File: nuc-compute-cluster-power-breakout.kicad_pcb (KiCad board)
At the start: 4 copper layers, 100 x 100 mm, 159 parts, among them J1 USB3106-30-0230-A, J10 10107844-002LF, J2 BM04B-SRSS-TB-LF-SN, J3 BM04B-SRSS-TB-LF-SN, J4 43045-1013, J5 430450812, J6 430450812, J7 430450812, J8 430450812, J9 430450812, Q1 SQS401EN-T1_BE3, Q10 SSM3K15ACT, Q11 BC856,215, Q15 DMN4010LFG-7, Q2 SQS401EN-T1_BE3, Q3 SSM3K15ACT, Q4 SSM3K15ACT, Q5 SQS401EN-T1_BE3, Q6 SSM3K15ACT, Q7 SQS401EN-T1_BE3, Q8 SQS401EN-T1_BE3, Q9 SSM3K15ACT, U1 FT2232HL-REEL, U10 TCA9534, U11 TMCS1100A2-Q1, U12 TMCS1100A2-Q1, U13 TMCS1100A2-Q1, U14 ADS7828, U15 AP62301WU-7, U7 AP62301WU-7, U8 TMCS1100A2-Q1, U9 TMCS1100A2-Q1, Y1 KX-7_12,MHz

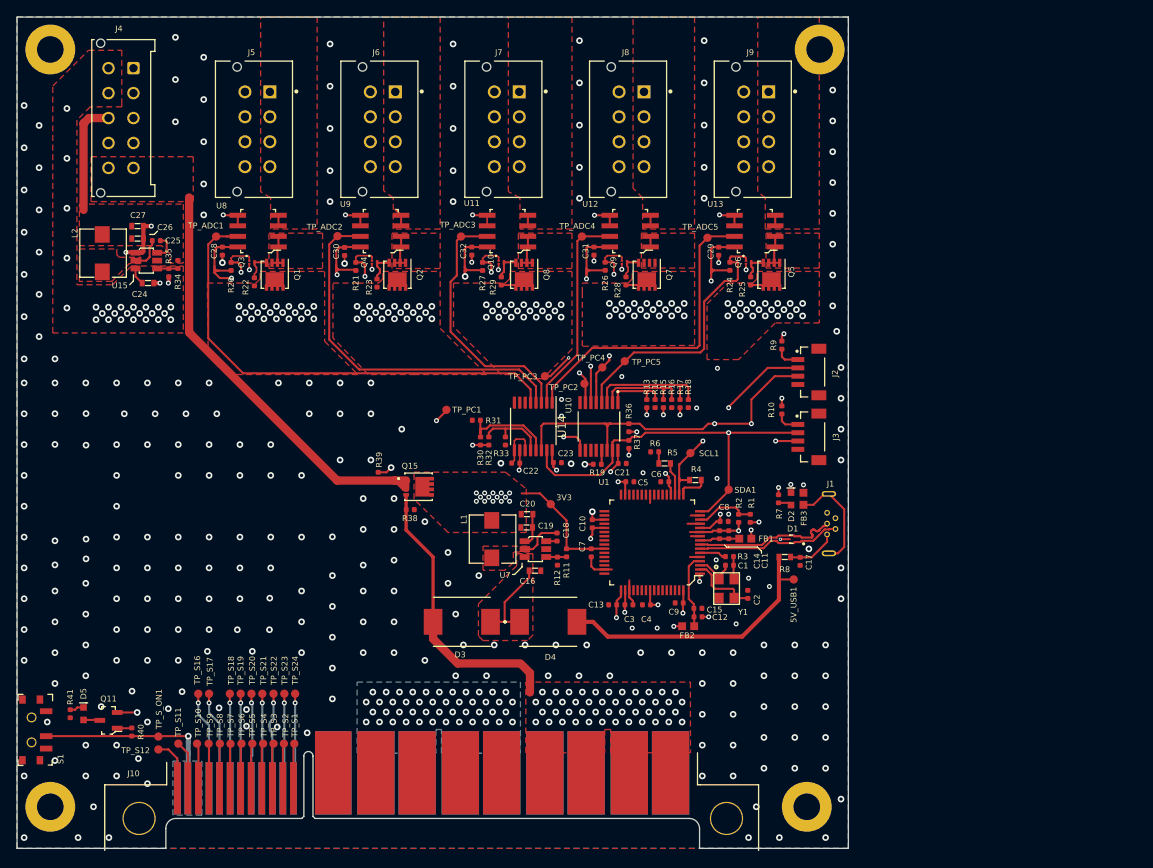
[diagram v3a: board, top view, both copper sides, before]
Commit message: Initial galvanic isolation added to layout
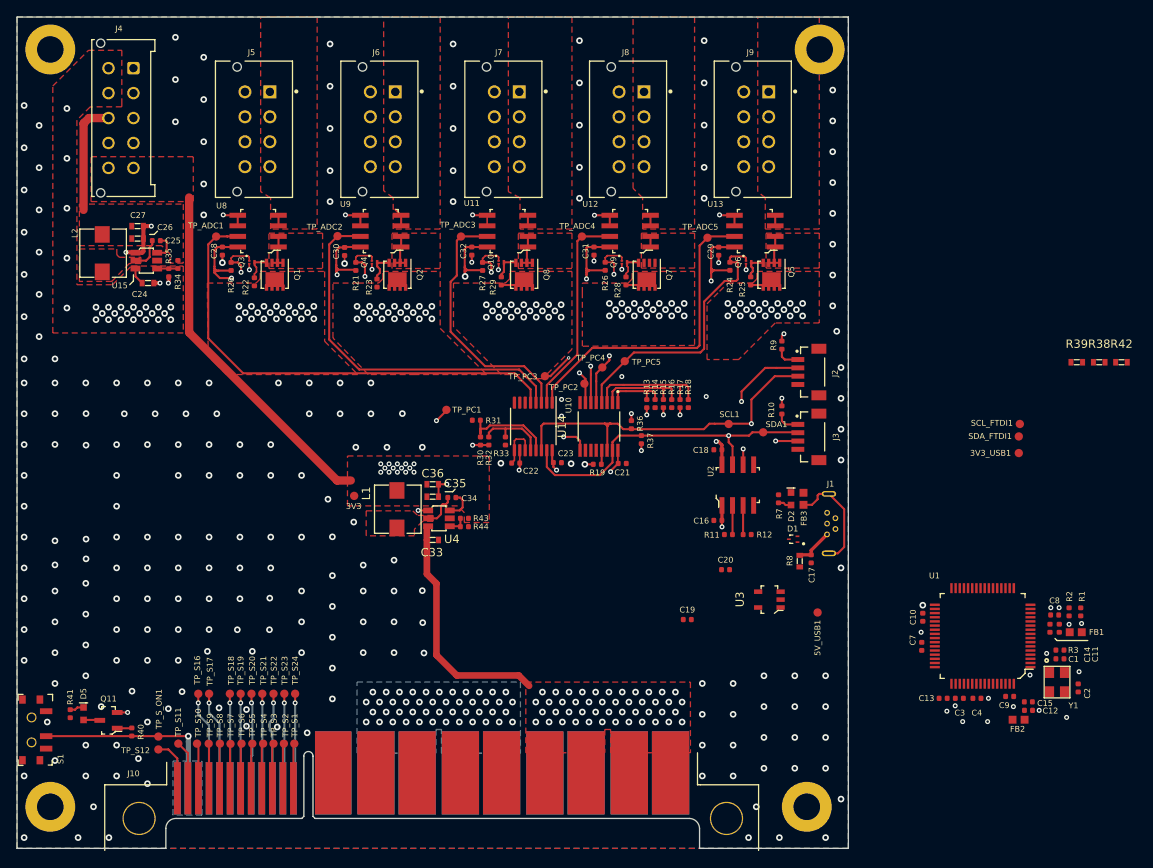
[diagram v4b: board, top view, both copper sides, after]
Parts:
- removed C5, C6: C_100n_0402, nuc-compute-cluster-power-breakout-footprints:0402-cap
- removed D3, D4: MBRS330T3G, nuc-compute-cluster-power-breakout-footprints:MBRS340T3
- removed Q15: DMN4010LFG-7, nuc-compute-cluster-power-breakout-footprints:POWERVDFN-8
- removed R4, R5: R_0R_0603, nuc-compute-cluster-power-breakout-footprints:0603-res
- removed R6: R_220R_0402, nuc-compute-cluster-power-breakout-footprints:0402-res
- removed U7: AP62301WU-7, nuc-compute-cluster-power-breakout-footprints:TSOT23-6
- added 3V3_USB1: TP_SMD1MM, nuc-compute-cluster-power-breakout-footprints:Testpoint_smd_1mm, F.Cu at (210.5, 102.5)
- added C33: C_10u_16V_0603, nuc-compute-cluster-power-breakout-footprints:0603-cap, F.Cu at (140.0, 112.9)
- added C34: C_100n_0402, nuc-compute-cluster-power-breakout-footprints:0402-cap, F.Cu at (142.3, 107.8)
- added C35: C_22u_0603, nuc-compute-cluster-power-breakout-footprints:0603-cap, F.Cu at (140.0, 107.7)
- added C36: C_22u_0603, nuc-compute-cluster-power-breakout-footprints:0603-cap, F.Cu at (140.0, 106.2)
- added R42: R_0R_0603, nuc-compute-cluster-power-breakout-footprints:0603-res, F.Cu at (222.8, 91.5)
- added R43: R_31k6_0402, nuc-compute-cluster-power-breakout-footprints:0402-res, F.Cu at (143.8, 110.3)
- added R44: R_10k_0402, nuc-compute-cluster-power-breakout-footprints:0402-res, F.Cu at (143.8, 111.3)
- added SCL_FTDI1: TP_SMD1MM, nuc-compute-cluster-power-breakout-footprints:Testpoint_smd_1mm, F.Cu at (210.6, 99.0)
- added SDA_FTDI1: TP_SMD1MM, nuc-compute-cluster-power-breakout-footprints:Testpoint_smd_1mm, F.Cu at (210.5, 100.5)
- added U2: ISO1641, antmicro-footprints:SOIC-8_W3.9mm, F.Cu at (176.7, 106.3)
- added U3: NCP163ASN330T1G, antmicro-footprints:SOT-23-5, F.Cu at (180.5, 120.1)
- added U4: AP62301WU-7, nuc-compute-cluster-power-breakout-footprints:TSOT23-6, F.Cu at (140.8, 110.3)
- C16: value C_10u_16V_0603 -> C_100n_0402; footprint nuc-compute-cluster-power-breakout-footprints:0603-cap -> antmicro-footprints:0402-cap
- C18: footprint nuc-compute-cluster-power-breakout-footprints:0402-cap -> antmicro-footprints:0402-cap
- C19, C20: value C_22u_0603 -> C_1u_0402; footprint nuc-compute-cluster-power-breakout-footprints:0603-cap -> antmicro-footprints:0402-cap
- R11: value R_31k6_0402 -> R_1k5_0402; footprint nuc-compute-cluster-power-breakout-footprints:0402-res -> antmicro-footprints:0402-res
- R12: value R_10k_0402 -> R_1k5_0402; footprint nuc-compute-cluster-power-breakout-footprints:0402-res -> antmicro-footprints:0402-res
- R36, R37: value R_4k7_0402 -> R_1k5_0402; footprint nuc-compute-cluster-power-breakout-footprints:0402-res -> antmicro-footprints:0402-res
- R38, R39: value R_10k_0402 -> R_0R_0603; footprint nuc-compute-cluster-power-breakout-footprints:0402-res -> nuc-compute-cluster-power-breakout-footprints:0603-res
- moved R39 85.1 mm to (217.5, 91.5), turned to 0 degrees
- moved R38 84.7 mm to (220.2, 91.5)
- moved C1 41.3 mm to (215.4, 127.2)
- moved C10 41.3 mm to (198.9, 122.2)
- moved C11 41.3 mm to (215.4, 123.5)
- moved C12 41.3 mm to (211.7, 133.4)
- moved C13 41.3 mm to (201.4, 131.9)
- moved C14 41.3 mm to (214.2, 123.5)
- moved C15 41.3 mm to (211.7, 132.4)
- moved C2 41.3 mm to (217.7, 130.7)
- moved C3 41.3 mm to (203.3, 131.9)
- moved C4 41.3 mm to (205.5, 131.9)
- moved C7 41.3 mm to (198.8, 125.7)
- moved C8 41.3 mm to (214.8, 121.9)
- moved C9 41.3 mm to (209.4, 131.7)
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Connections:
- C1 pad 2: GND -> GNDD
- C10 pad 2: GND -> GNDD
- C11 pad 2: GND -> GNDD
- C12 pad 2: GND -> GNDD
- C13 pad 2: GND -> GNDD
- C14 pad 2: GND -> GNDD
- C15 pad 2: GND -> GNDD
- C16 pad 1: Net-(C16-Pad1) -> VCC3V3_USB
- C16 pad 2: GND -> GNDD
- C17 pad 2: GND -> GNDD
- C18 pad 1: Net-(C18-Pad1) -> VCC3V3
- C18 pad 2: Net-(C18-Pad2) -> GND
- C19 pad 1: VCC3V3 -> VCC5V0_USB
- C19 pad 2: GND -> GNDD
- C2 pad 2: GND -> GNDD
- C20 pad 1: VCC3V3 -> VCC3V3_USB
- C20 pad 2: GND -> GNDD
- C3 pad 1: VCC3V3 -> VCC3V3_USB
- C3 pad 2: GND -> GNDD
- C4 pad 1: VCC3V3 -> VCC3V3_USB
- C4 pad 2: GND -> GNDD
- C7 pad 1: VCC3V3 -> VCC3V3_USB
- C7 pad 2: GND -> GNDD
- C8 pad 2: GND -> GNDD
- C9 pad 2: GND -> GNDD
- D1 pad 3: GND -> GNDD
- D2 pad 2: GND -> GNDD
- FB1 pad 2: VCC3V3 -> VCC3V3_USB
- FB2 pad 2: VCC3V3 -> VCC3V3_USB
- FB3 pad 2: GND -> GNDD
- J1 pad 4: (no net) -> Net-(J1-Pad4)
- J1 pad 5: GND -> GNDD
- J10 pad P19/20: (no net) -> Net-(J10-PadP19/20)
- J4 pad 10: DB_3V3 -> VCC3V3
- J4 pad 5: DB_3V3 -> VCC3V3
- L1 pad 1: Net-(C18-Pad1) -> Net-(C34-Pad1)
- R1 pad 1: VCC3V3 -> VCC3V3_USB
- R11 pad 1: VCC3V3 -> VCC3V3_USB
- R11 pad 2: Net-(R11-Pad2) -> SDA_FTDI
- R12 pad 1: Net-(R11-Pad2) -> VCC3V3_USB
- R12 pad 2: GND -> SCL_FTDI
- R2 pad 2: GND -> GNDD
- R3 pad 1: GND -> GNDD
- R38 pad 1: VCC12V0 -> SDA_FTDI
- R38 pad 2: GND -> SDA
- R39 pad 1: DB_3V3 -> SCL_FTDI
- R39 pad 2: GND -> SCL
- R7 pad 1: VCC3V3 -> VCC3V3_USB
- S1 pad 1: (no net) -> Net-(S1-Pad1)
- U1 pad 1: GND -> GNDD
- U1 pad 10: GND -> GNDD
- U1 pad 11: GND -> GNDD
- U1 pad 13: GND -> GNDD
- U1 pad 15: GND -> GNDD
- U1 pad 20: VCC3V3 -> VCC3V3_USB
- U1 pad 21: (no net) -> Net-(U1-Pad21)
- U1 pad 22: (no net) -> Net-(U1-Pad22)
- U1 pad 23: (no net) -> Net-(U1-Pad23)
- U1 pad 24: (no net) -> Net-(U1-Pad24)
- U1 pad 25: GND -> GNDD
- U1 pad 26: (no net) -> Net-(U1-Pad26)
- U1 pad 27: (no net) -> Net-(U1-Pad27)
- U1 pad 28: (no net) -> Net-(U1-Pad28)
- U1 pad 29: (no net) -> Net-(U1-Pad29)
- U1 pad 30: (no net) -> Net-(U1-Pad30)
- U1 pad 31: VCC3V3 -> VCC3V3_USB
- U1 pad 32: (no net) -> Net-(U1-Pad32)
- U1 pad 33: (no net) -> Net-(U1-Pad33)
- U1 pad 34: (no net) -> Net-(U1-Pad34)
- U1 pad 35: GND -> GNDD
- U1 pad 36: (no net) -> Net-(U1-Pad36)
- U1 pad 38: (no net) -> Net-(U1-Pad38)
- U1 pad 39: (no net) -> Net-(U1-Pad39)
- U1 pad 40: (no net) -> Net-(U1-Pad40)
- U1 pad 41: (no net) -> Net-(U1-Pad41)
- U1 pad 42: VCC3V3 -> VCC3V3_USB
- U1 pad 43: (no net) -> Net-(U1-Pad43)
- U1 pad 44: (no net) -> Net-(U1-Pad44)
- U1 pad 45: (no net) -> Net-(U1-Pad45)
- U1 pad 46: (no net) -> Net-(U1-Pad46)
- U1 pad 47: GND -> GNDD
- U1 pad 48: (no net) -> Net-(U1-Pad48)
- U1 pad 5: GND -> GNDD
- U1 pad 50: VCC3V3 -> VCC3V3_USB
- U1 pad 51: GND -> GNDD
- U1 pad 52: (no net) -> Net-(U1-Pad52)
- U1 pad 53: (no net) -> Net-(U1-Pad53)
- U1 pad 54: (no net) -> Net-(U1-Pad54)
- U1 pad 55: (no net) -> Net-(U1-Pad55)
- U1 pad 56: VCC3V3 -> VCC3V3_USB
- U1 pad 57: (no net) -> Net-(U1-Pad57)
- U1 pad 58: (no net) -> Net-(U1-Pad58)
- U1 pad 59: (no net) -> Net-(U1-Pad59)
- U1 pad 60: (no net) -> Net-(U1-Pad60)
- U1 pad 61: (no net) -> Net-(U1-Pad61)
- U1 pad 62: (no net) -> Net-(U1-Pad62)
- U1 pad 63: (no net) -> Net-(U1-Pad63)
- U10 pad 10: (no net) -> Net-(U10-Pad10)
- U10 pad 11: (no net) -> Net-(U10-Pad11)
- U10 pad 12: (no net) -> Net-(U10-Pad12)
- U14 pad 6: (no net) -> Net-(U14-Pad6)
- U14 pad 7: (no net) -> Net-(U14-Pad7)
- U14 pad 8: (no net) -> Net-(U14-Pad8)
- U15 pad 5: (no net) -> Net-(U15-Pad5)
- Y1 pad 2: GND -> GNDD
- Y1 pad 4: GND -> GNDD
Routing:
- net DB_3V3: track 54.2 -> 0.00 mm
- net 1V8_FT: track 48.1 -> 0.00 mm
- net VCC5V0_USB: track 34.2 -> 0.00 mm
- net VCC3V3: track 189.5 -> 157.6 mm, vias 42 -> 34
- net GND: track 86.9 -> 56.9 mm, vias 325 -> 293
- net /FTDI/USB_D+: track 17.5 -> 0.00 mm
- net /FTDI/USB_D-: track 17.5 -> 0.00 mm
- net Net-(C16-Pad1): track 10.9 -> 0.00 mm
- net Net-(C12-Pad1): track 9.08 -> 0.00 mm
- net OSCI: track 8.59 -> 0.00 mm
- net /FTDI/FTDI_RST: track 7.26 -> 0.00 mm
- net SCL: track 61.7 -> 54.4 mm, vias 4 -> 3
- net SDA: track 61.0 -> 53.8 mm
- net VCC12V0: track 63.2 -> 57.4 mm
- net Net-(C18-Pad1): track 5.23 -> 0.00 mm
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- added copper zone on F.Cu, net Net-(C34-Pad1)
- removed copper zone on F.Cu, net DB_3V3
- removed copper zone on F.Cu, net Net-(C16-Pad1)
- removed copper zone on F.Cu, net Net-(C18-Pad1)

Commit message: Complete galvanic isolated layout
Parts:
- added C5: C_100n_0402, nuc-compute-cluster-power-breakout-footprints:0402-cap, F.Cu at (157.4, 111.5)
- added C6: C_100n_0402, nuc-compute-cluster-power-breakout-footprints:0402-cap, F.Cu at (157.2, 126.4)
- added R4: R_0R_0603, nuc-compute-cluster-power-breakout-footprints:0603-res, F.Cu at (164.3, 111.3)
- added R5: R_0R_0603, nuc-compute-cluster-power-breakout-footprints:0603-res, F.Cu at (161.8, 109.8)
- added R6: R_220R_0402, nuc-compute-cluster-power-breakout-footprints:0402-res, F.Cu at (161.8, 108.5)
- moved C8 58.8 mm to (156.1, 126.4), turned to 270 degrees
- moved C4 53.9 mm to (152.9, 119.9), turned to 270 degrees
- moved R42 53.3 mm to (171.7, 106.2), turned to 90 degrees
- moved R3 50.0 mm to (165.4, 126.9), turned to 0 degrees
- moved R38 49.3 mm to (173.2, 106.2), turned to 90 degrees
- moved R1 48.1 mm to (170.3, 114.8), turned to 180 degrees
- moved R2 46.6 mm to (170.3, 115.8), turned to 0 degrees
- moved C2 46.4 mm to (171.6, 125.4), turned to 270 degrees
- moved FB1 46.4 mm to (171.5, 117.0)
- moved U1 46.4 mm to (160.2, 118.7)
- moved C3 46.3 mm to (161.8, 111.5), turned to 180 degrees
- moved C10 46.3 mm to (153.0, 116.5)
- moved C11 46.2 mm to (169.6, 117.3)
- moved Y1 46.2 mm to (169.3, 124.2)
- moved C14 46.1 mm to (168.6, 117.3)
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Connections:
- U1 pad 16: SDA -> SDA_FTDI
- U1 pad 18: SCL -> SCL_FTDI
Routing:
- net 1V8_FT: track 0.00 -> 40.2 mm
- net GNDD: track 0.00 -> 34.3 mm, vias 4 -> 7
- net /FTDI/USB_D-: track 0.00 -> 26.0 mm
- net /FTDI/USB_D+: track 0.00 -> 25.9 mm
- net SCL_FTDI: track 3.50 -> 26.9 mm, vias 0 -> 2
- net VCC3V3_USB: track 2.66 -> 20.4 mm, vias 4 -> 21
- net SDA_FTDI: track 3.50 -> 19.6 mm
- net OSCI: track 0.00 -> 8.79 mm
- net Net-(R3-Pad2): track 0.00 -> 8.33 mm
- net VCC5V0_USB: track 0.00 -> 7.94 mm
- net OSCO: track 0.00 -> 7.86 mm
- net Net-(C11-Pad1): track 0.00 -> 5.78 mm
- net /FTDI/FTDI_RST: track 0.00 -> 5.54 mm
- net SCL: track 54.4 -> 59.6 mm, vias 3 -> 2
- net Net-(C12-Pad1): track 0.00 -> 4.57 mm
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- added copper zone on F.Cu, net GNDD
- added copper zone on F.Cu, net VCC3V3_USB
- added copper zone on In2.Cu, net VCC3V3_USB

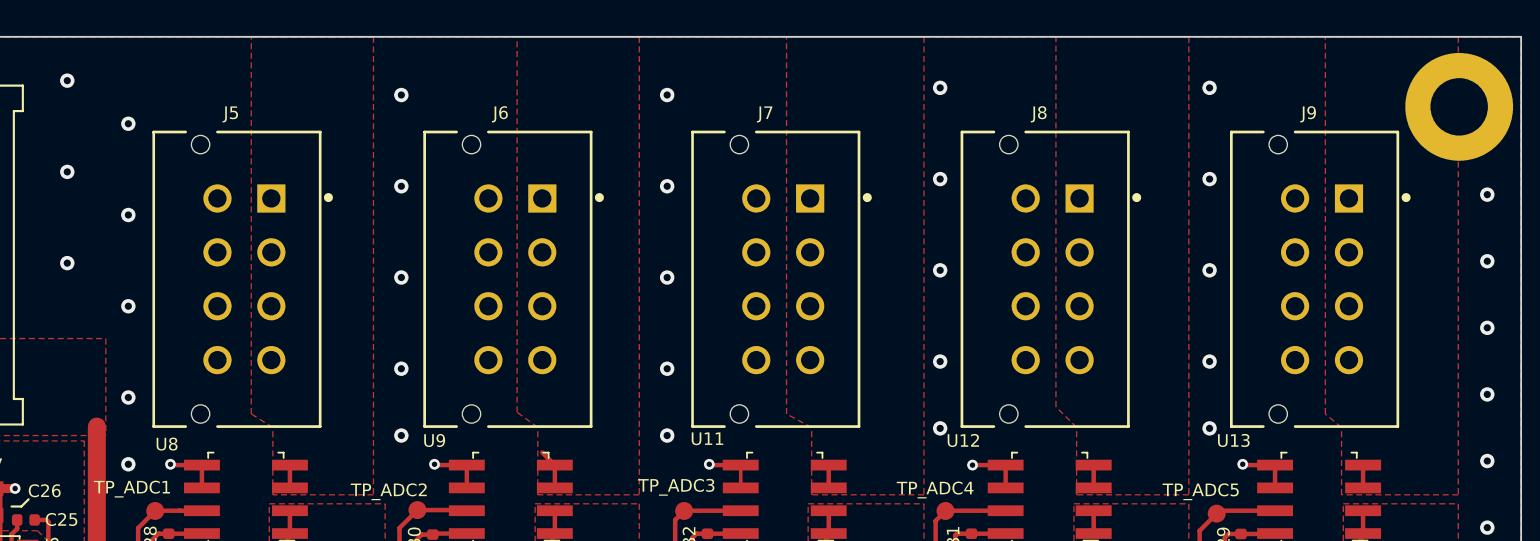
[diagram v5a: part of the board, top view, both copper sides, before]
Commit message: Label output channel names
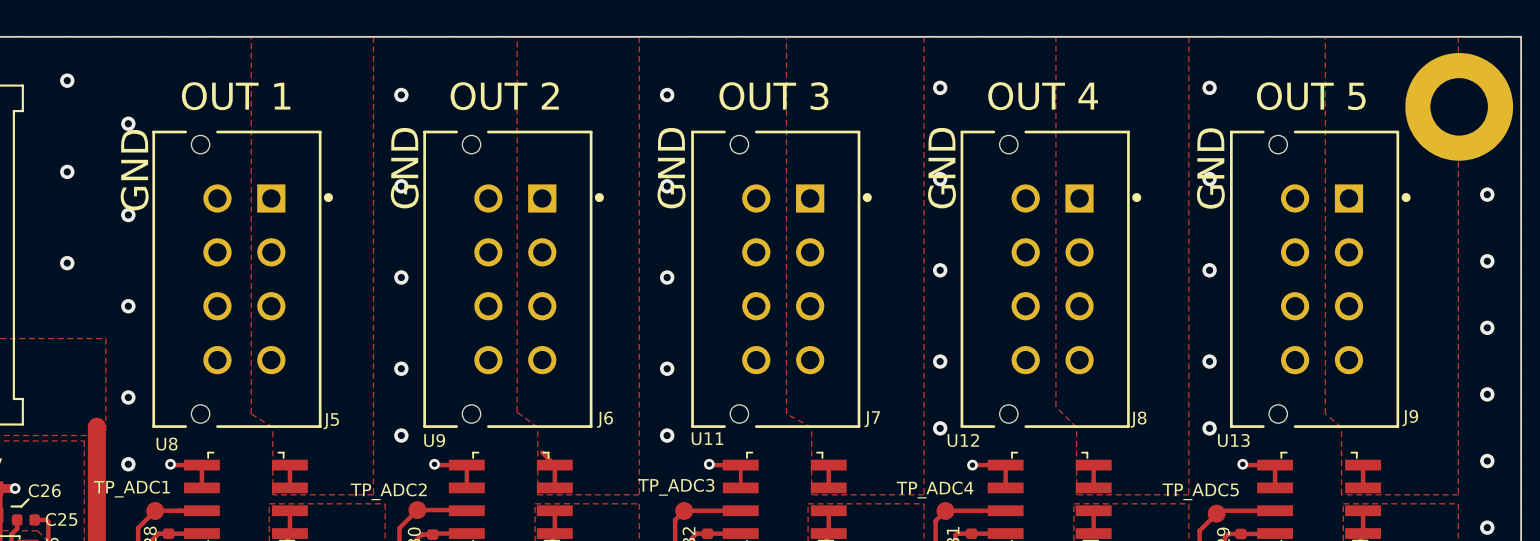
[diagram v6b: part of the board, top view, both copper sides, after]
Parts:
- moved N1 0.51 mm to (96.1, 108.2)
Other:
- board text added: "GND"
- board text added: "OUT 1"
- board text added: "OUT 2"
- board text added: "OUT 3"
- board text added: "OUT 4"
- board text added: "OUT 5"
- board text added: "Server PSU Breakout"
- board text removed: "Server PSU Breakout Board"

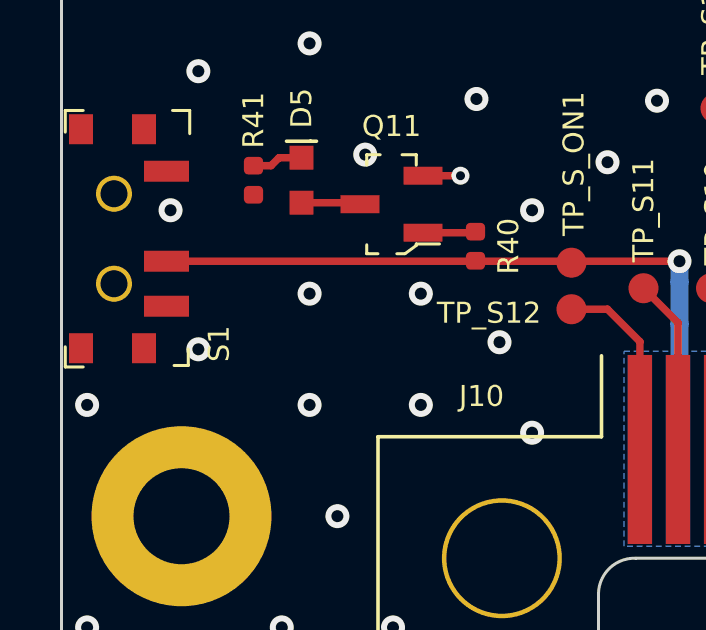
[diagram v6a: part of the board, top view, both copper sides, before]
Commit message: Add R45 to implement ALWAYS ON feature
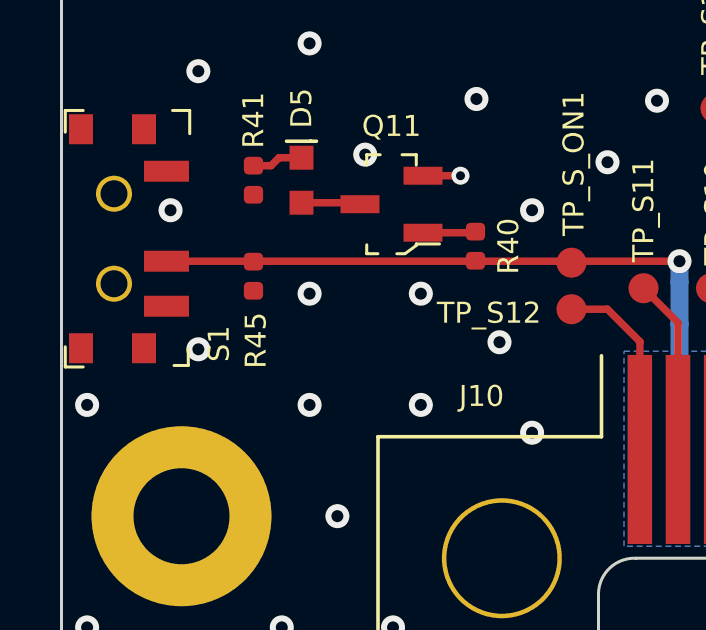
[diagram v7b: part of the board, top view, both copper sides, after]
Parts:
- added R45: R_0R_0402, nuc-compute-cluster-power-breakout-footprints:0402-res, F.Cu at (96.4, 137.0)
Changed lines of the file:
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@@
     (tracks 1451)
     (zones 0)
-    (modules 168)
+    (modules 169)
     (nets 135)
   )
@@
     (45 Margin user hide)
     (46 B.CrtYd user hide)
-    (47 F.CrtYd user hide)
+    (47 F.CrtYd user)
     (48 B.Fab user hide)
     (49 F.Fab user hide)
@@
     (add_net /FTDI/USB_D-)
   )
+  (module nuc-compute-cluster-power-breakout-footprints:0402-res (layer F.Cu)
+    (at 96.4 137 90)
+    (descr "Resistor SMD 0402 (1005 Metric), square (rectangular) end terminal, IPC_7351 nominal, (Body size source: http://www.tortai-tech.com/upload/download/2011102023233369053.pdf), generated with kicad-footprint-generator")
+    (tags resistor)
+    (attr smd)
+    (fp_text reference R45 (at -2.14 0.08 90) (layer F.SilkS)
+      (effects (font (size 0.7 0.7) (thickness 0.15)))
+    )
+    (fp_text value R_0R_0402 (at 0 1.17 90) (layer F.Fab)
+      (effects (font (size 1 1) (thickness 0.15)))
+    )
+    (fp_text user %R (at 0 0 90) (layer F.Fab)
+      (effects (font (size 0.25 0.25) (thickness 0.04)))
+    )
+    (fp_line (start 0.93 0.47) (end -0.93 0.47) (layer F.CrtYd) (width 0.05))
+    (fp_line (start 0.93 -0.47) (end 0.93 0.47) (layer F.CrtYd) (width 0.05))
+    (fp_line (start -0.93 -0.47) (end 0.93 -0.47) (layer F.CrtYd) (width 0.05))
+    (fp_line (start -0.93 0.47) (end -0.93 -0.47) (layer F.CrtYd) (width 0.05))
+    (fp_line (start 0.5 0.25) (end -0.5 0.25) (layer F.Fab) (width 0.1))
+    (fp_line (start 0.5 -0.25) (end 0.5 0.25) (layer F.Fab) (width 0.1))
+    (fp_line (start -0.5 -0.25) (end 0.5 -0.25) (layer F.Fab) (width 0.1))
+    (fp_line (start -0.5 0.25) (end -0.5 -0.25) (layer F.Fab) (width 0.1))
+    (pad 2 smd roundrect (at 0.485 0 90) (size 0.59 0.64) (layers F.Cu F.Paste F.Mask) (roundrect_rratio 0.25)
+      (net 58 PSU_ON))
+    (pad 1 smd roundrect (at -0.485 0 90) (size 0.59 0.64) (layers F.Cu F.Paste F.Mask) (roundrect_rratio 0.25)
+      (net 4 GND))
+    (model ${KIPRJMOD}/lib/3d-models/0402-res.step
+      (offset (xyz 0 0 -0.01))
+      (scale (xyz 1 1 1))
+      (rotate (xyz 0 0 0))
+    )
+  )
   (module nuc-compute-cluster-power-breakout-footprints:KX-7 (layer F.Cu)
